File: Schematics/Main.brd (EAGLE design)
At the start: 160 x 100 mm, 15 parts, among them U1 LCD-16X2SILK, X1 USBPTH

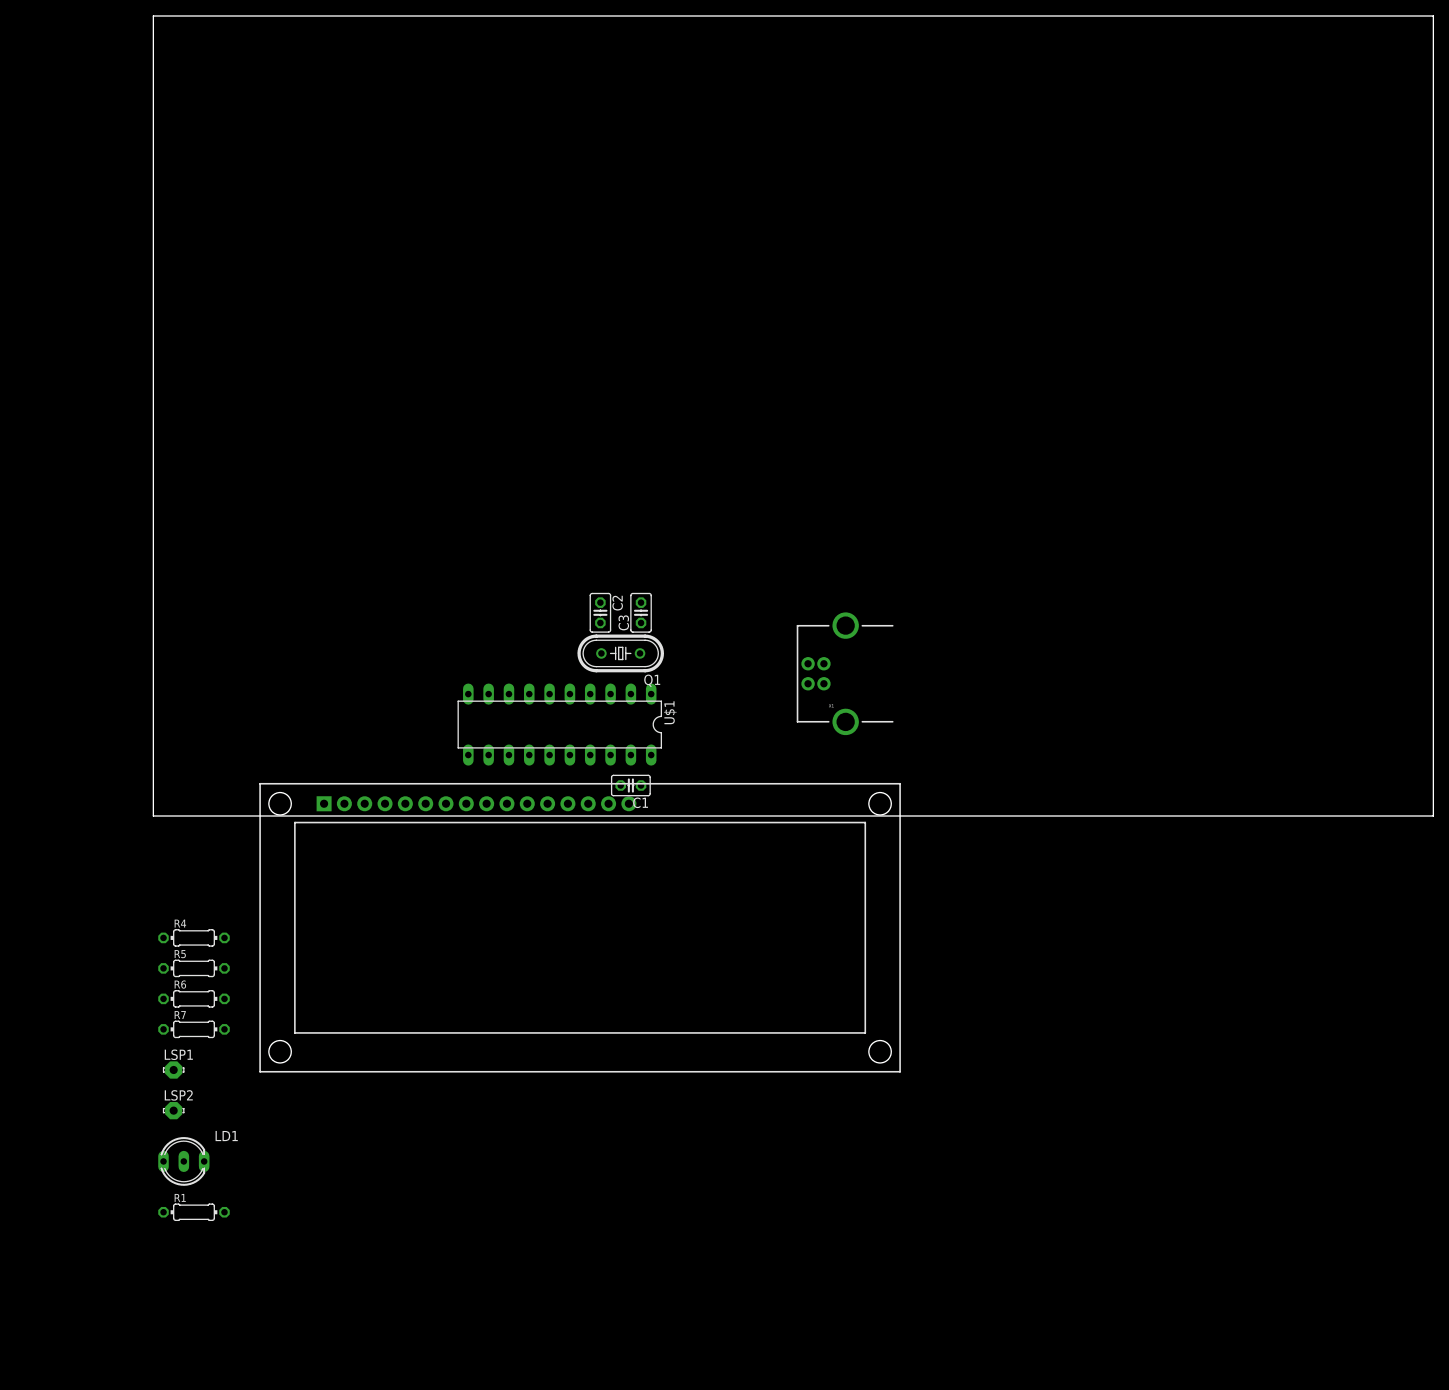
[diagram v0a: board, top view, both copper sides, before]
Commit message: Schematic complete
Board nearly complete, only one route missing. Will see if 2 resistors are enough to condition the signal.

Signed-off-by: Aljaž Srebrnič <a2piratesoft@gmail.com>
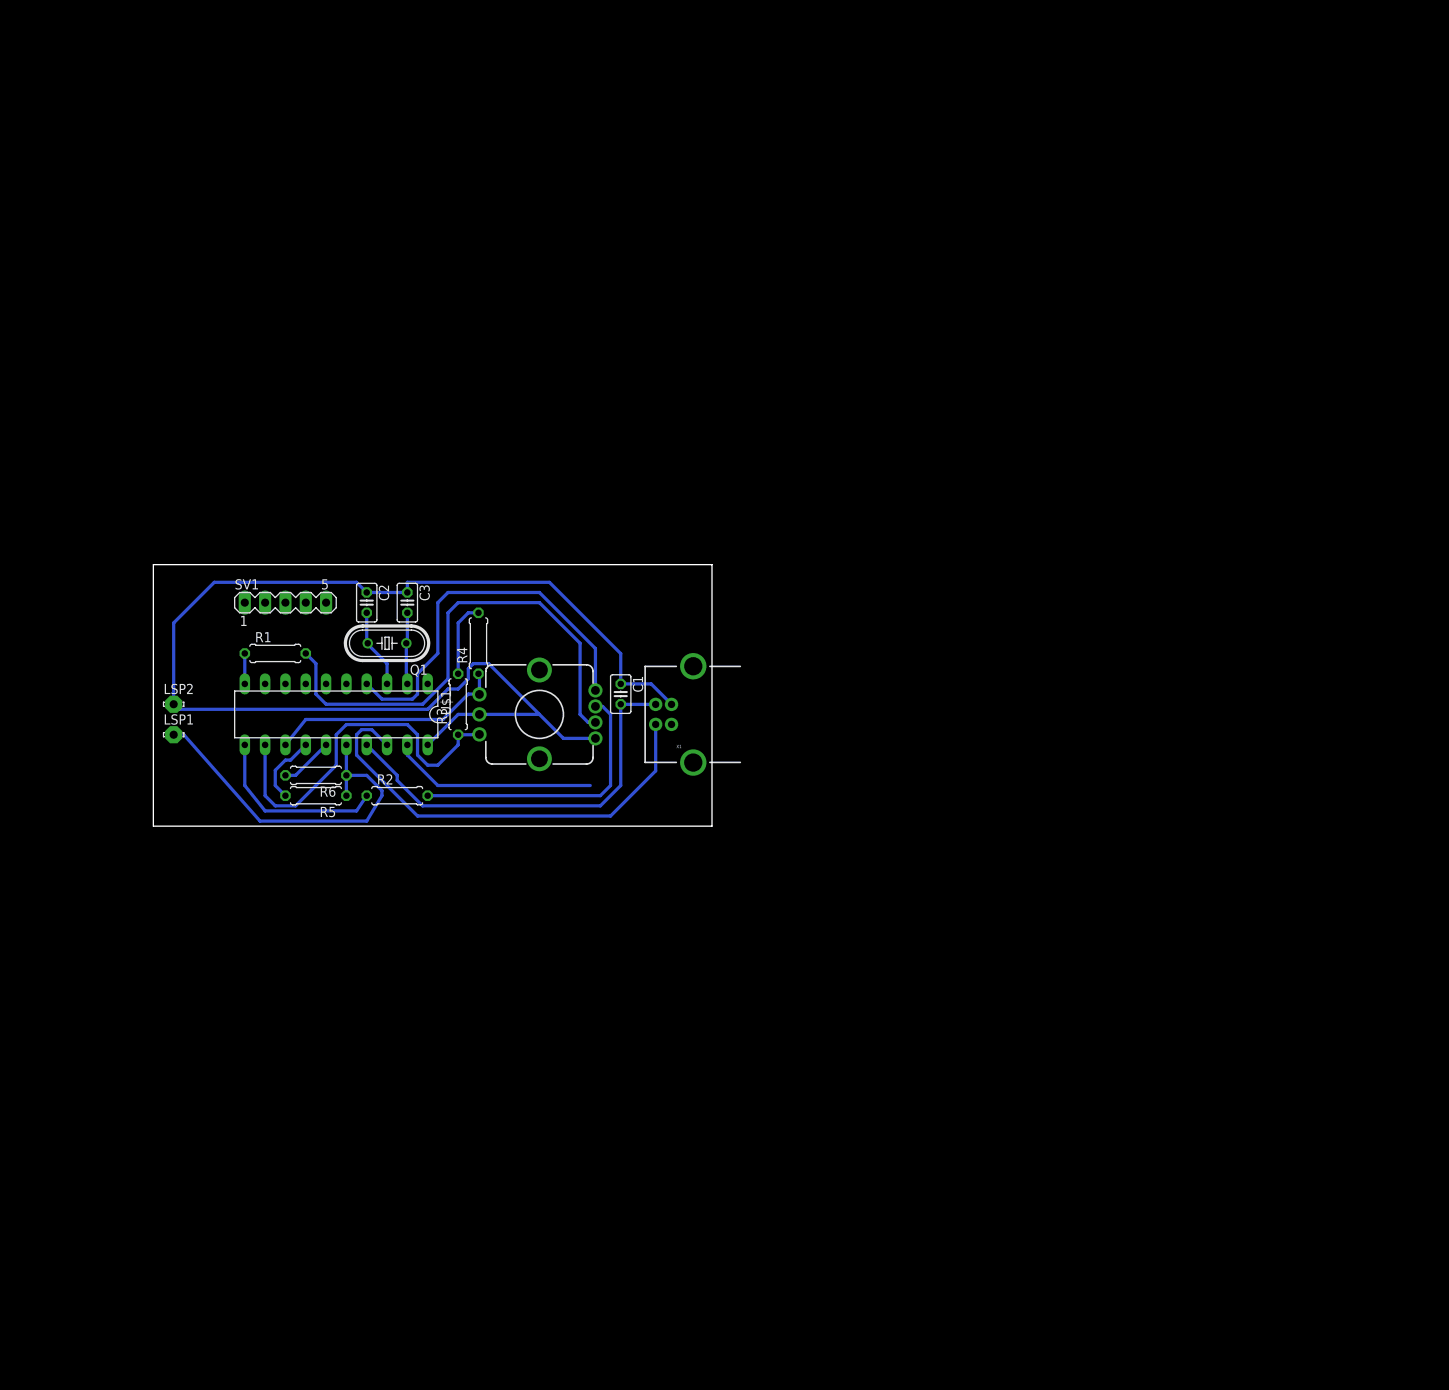
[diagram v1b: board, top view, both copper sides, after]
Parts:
- removed LD1: (no value), led:DUOLED-C-5MM
- removed R7: (no value), rcl:0204/7
- added R2: 470, rcl:0207/7
- added R3: 10k, rcl:0207/7
- added SV1: (no value), con-lstb:MA05-1
- R1, R5, R6: device rcl:0204/7 -> rcl:0207/7
- R4: value (none) -> 10k; device rcl:0204/7 -> rcl:0207/7
- U1: value LCD-16X2SILK -> ENCODER_2LED; device SparkFun:LCD-16X2 -> SparkFun:ENCODER_LED_2
- moved R1 70.6 mm to (15.2, 20.3)
- moved R4 51.2 mm to (40.6, 21.6), turned to 90 degrees
- moved LSP2 50.8 mm to (2.54, 14.0)
- moved LSP1 41.9 mm to (2.54, 10.2)
- moved R6 31.8 mm to (20.3, 5.08), turned to 180 degrees
- moved C2 29.2 mm to (26.7, 26.7)
- moved C3 29.2 mm to (31.8, 26.7), turned to 270 degrees
- moved Q1 29.2 mm to (29.2, 21.6)
- moved U$1 28.0 mm to (36.8, 17.8)
- moved U1 27.1 mm to (48.3, 12.7), turned to 270 degrees
- moved R5 26.4 mm to (20.3, 2.54), turned to 180 degrees
- moved X1 19.7 mm to (64.8, 12.7)
- moved C1 11.5 mm to (58.4, 15.2), turned to 270 degrees
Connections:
- removed net A: U1.15
- removed net DB4: U$1.13, U1.11
- removed net DB5: U$1.12, U1.12
- removed net DB6: U$1.11, U1.13
- removed net DB7: U$1.10, U1.14
- removed net E: U$1.14, U1.6
- removed net K: U1.16
- removed net R/W: U$1.15, U1.5
- removed net RS: U$1.16, U1.4
- new net D/~C: U$1.5
- new net N$10: R2.1, U$1.11
- new net N$11: R3.1, U$1.12, U1.B
- new net N$14: R5.2, U$1.14
- new net SCLK: U$1.8
- new net SDIN: U$1.9
- new net ~RES: U$1.7
- new net ~SCE: U$1.6
- net GND: now also U1.C, U1.GND; no longer LD1.AX, U1.1
- net N$12: now also U$1.13, U1.A; no longer LSP1.MP, R5.1, R6.1, R7.1
- net N$13: now also R6.2, U$1.15; no longer R1.1, U$1.4
- net N$5: now also U$1.4, U1.SW; no longer R7.2, U$1.9
- net N$6: now also R1.1, U$1.10; no longer R6.2, U$1.8
- net N$7: now also R1.2, U1.+G; no longer R5.2, U$1.5, U$1.6
- net N$8: now also LSP1.MP, R5.1, R6.1, U$1.16; no longer R4.2, U$1.7
- net N$9: now also R2.2, U1.+R; no longer LD1.C, R1.2
- net VDD: now also R3.2, R4.2; no longer LD1.AR, U1.2
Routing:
- net GND: track 0.00 -> 160.4 mm
- net N$7: track 0.00 -> 62.6 mm
- net N$3: track 0.00 -> 56.1 mm
- net VCC/2: track 0.00 -> 50.9 mm
- net N$5: track 0.00 -> 48.2 mm
- net N$11: track 0.00 -> 46.1 mm
- net N$8: track 0.00 -> 44.9 mm
- net N$9: track 0.00 -> 34.6 mm
- net N$12: track 0.00 -> 29.8 mm
- net N$2: track 0.00 -> 25.7 mm
- net N$10: track 0.00 -> 22.9 mm
- net N$1: track 0.00 -> 9.94 mm
- net VDD: track 0.00 -> 9.42 mm
- net N$4: track 0.00 -> 9.00 mm
- net N$14: track 0.00 -> 8.83 mm
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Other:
- board size 160 x 100 mm -> 69.8 x 32.7 mm

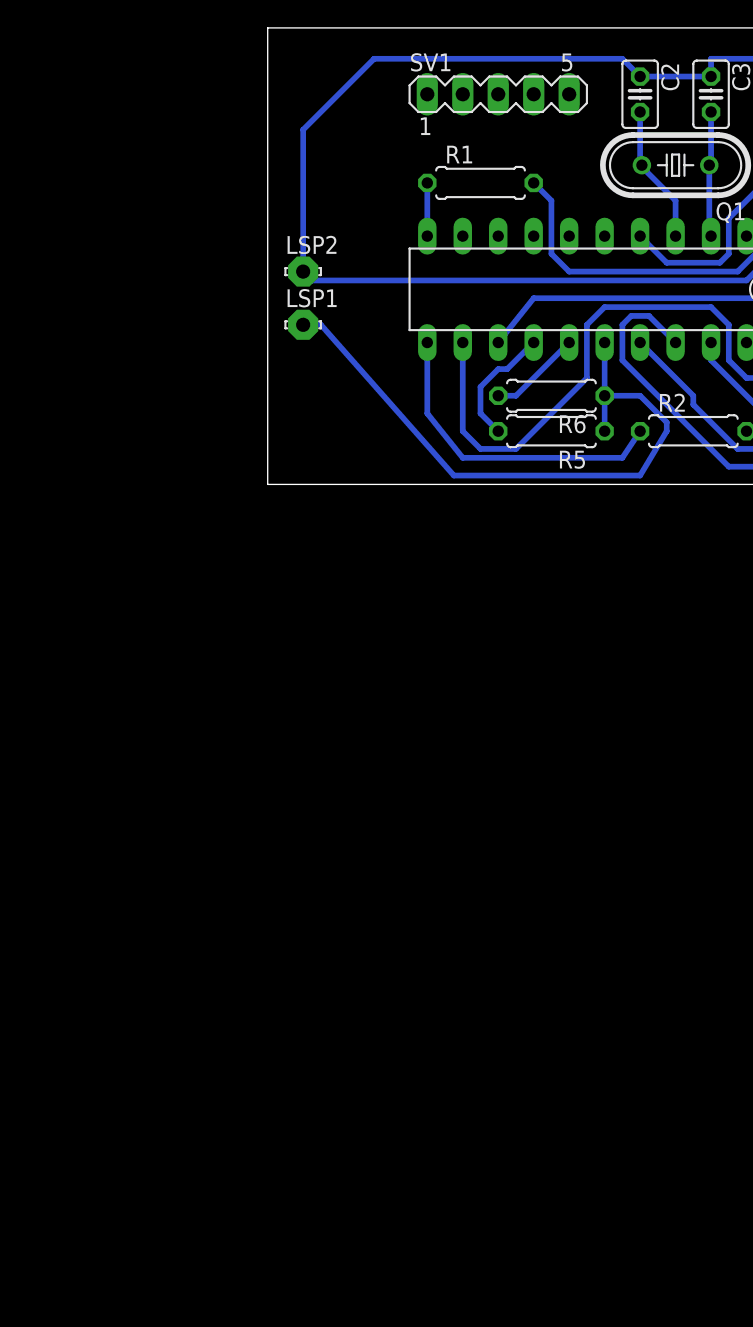
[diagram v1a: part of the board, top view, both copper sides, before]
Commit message: Schematics competed
Updated to use rotary encoder and nokia graphic screen.

Signed-off-by: Aljaž Srebrnič <a2piratesoft@gmail.com>
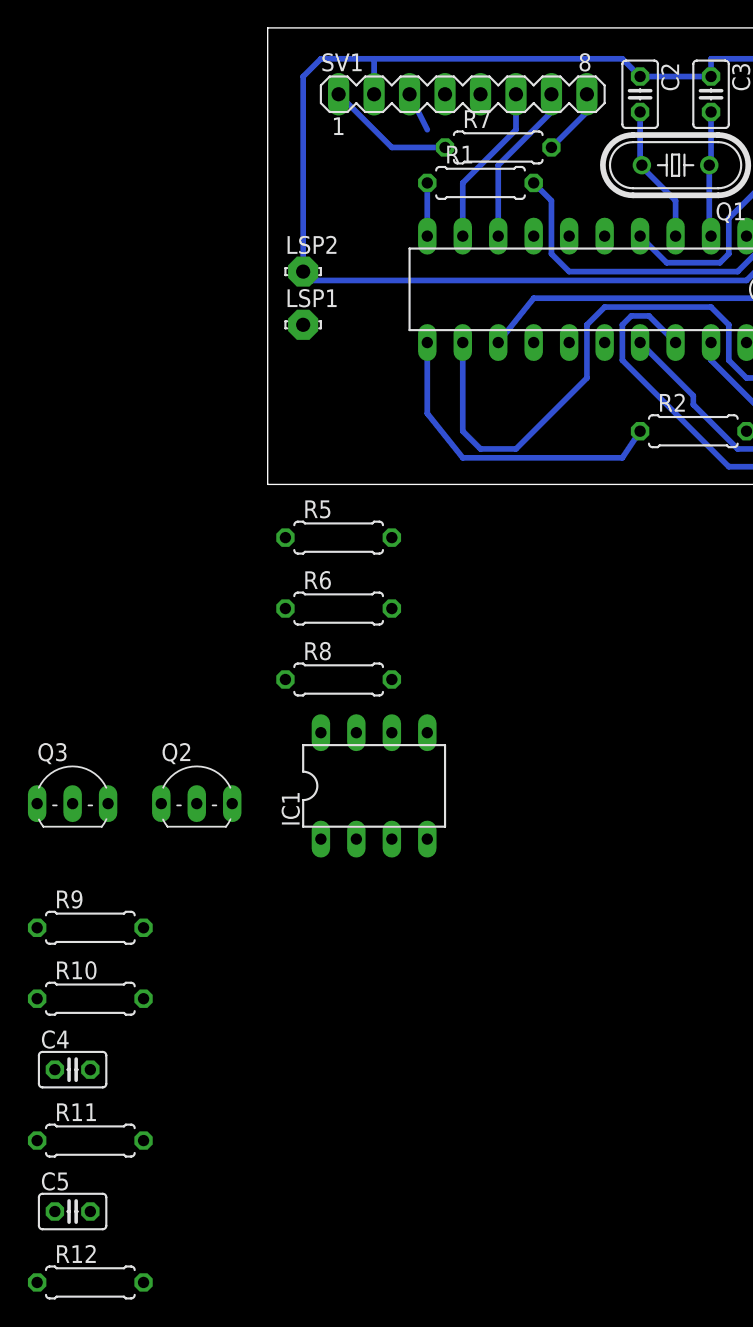
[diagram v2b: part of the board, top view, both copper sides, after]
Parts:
- added C4, C5: (no value), rcl:C025-025X050
- added IC1: ICL7611ACPA, maxim:DIL08
- added Q2, Q3: 2N5486, transistor-fet:TO92-
- added R10, R11, R12, R8, R9: (no value), rcl:0207/7
- added R7: 81, rcl:0207/7
- R1, R2: value 470 -> 81
- SV1: device con-lstb:MA05-1 -> con-lstb:MA08-1
- moved R6 21.6 mm to (5.08, -10.2), turned to 0 degrees
- moved R5 17.0 mm to (5.08, -5.08), turned to 0 degrees
- moved SV1 2.54 mm to (14.0, 26.7)
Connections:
- new net N$15: R7.2, SV1.8
- new net N$16: IC1.6, R8.2, U$1.15
- new net N$17: R10.1, R9.1, U$1.14
- new net N$18: R11.1, R12.1, U$1.7
- new net N$19: C4.1, Q2.1, R10.2
- new net N$20: C5.1, Q3.1, R12.2
- new net V+: IC1.7
- new net V-: IC1.4
- net D/~C: now also SV1.5
- net GND: now also C4.2, C5.2, IC1.3, Q2.2, SV1.2
- net N$13: now also IC1.2, R8.1; no longer U$1.15
- net N$14: now also LSP1.MP, Q3.2, R5.1; no longer R5.2, U$1.14
- net N$8: now also Q2.3, R5.2; no longer LSP1.MP, R5.1, U$1.16
- net SCLK: now also SV1.7
- net SDIN: now also SV1.6
- net VDD: now also Q3.3, R11.2, R7.1, R9.2, SV1.1
- net ~RES: now also SV1.4, U$1.16; no longer U$1.7
- net ~SCE: now also SV1.3
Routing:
- net N$8: track 44.9 -> 0.00 mm
- net SDIN: track 0.00 -> 11.7 mm
- net SCLK: track 0.00 -> 11.7 mm
- net VDD: track 9.42 -> 18.6 mm
- net N$14: track 8.83 -> 0.00 mm
- net N$13: track 6.66 -> 0.00 mm
- net N$15: track 0.00 -> 4.86 mm
- net GND: track 160.4 -> 165.1 mm
- net ~SCE: track 0.00 -> 2.84 mm
